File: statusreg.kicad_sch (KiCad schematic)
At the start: 11 parts, among them SW4 SW_DIP_x08, U56 74HC688, U57 74HC573, U58 74HC541, U6 74HC32, U7 74HC14

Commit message: done the pcb layout + added the 1M ram bank project
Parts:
- C17: footprint Capacitor_THT:C_Disc_P2.54mm -> Capacitor_THT:C_Disc_D3.0mm_W1.6mm_P2.54mm
- U56, U57, U58: footprint Package_DIP:DIP-20_W7.62mm_Socket -> Package_DIP:DIP-20_W7.62mm
- U6, U7: footprint Package_DIP:DIP-14_W7.62mm_Socket -> Package_DIP:DIP-14_W7.62mm
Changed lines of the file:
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@@
 			)
 		)
-		(property "Footprint" "Package_DIP:DIP-20_W7.62mm_Socket"
+		(property "Footprint" "Package_DIP:DIP-20_W7.62mm"
 			(at 215.9 76.2 0)
 			(effects
@@
 			)
 		)
-		(property "Footprint" "Package_DIP:DIP-20_W7.62mm_Socket"
+		(property "Footprint" "Package_DIP:DIP-20_W7.62mm"
 			(at 152.4 76.2 0)
 			(effects
@@
 			)
 		)
-		(property "Footprint" "Package_DIP:DIP-20_W7.62mm_Socket"
+		(property "Footprint" "Package_DIP:DIP-20_W7.62mm"
 			(at 88.9 76.2 0)
 			(effects
@@
 			)
 		)
-		(property "Footprint" "Capacitor_THT:C_Disc_P2.54mm"
+		(property "Footprint" "Capacitor_THT:C_Disc_D3.0mm_W1.6mm_P2.54mm"
 			(at 132.08 85.3948 0)
 			(effects
@@
 			)
 		)
-		(property "Footprint" "Package_DIP:DIP-14_W7.62mm_Socket"
+		(property "Footprint" "Package_DIP:DIP-14_W7.62mm"
 			(at 81.28 127 0)
 			(effects
@@
 			)
 		)
-		(property "Footprint" "Package_DIP:DIP-14_W7.62mm_Socket"
+		(property "Footprint" "Package_DIP:DIP-14_W7.62mm"
 			(at 96.52 127 0)
 			(effects

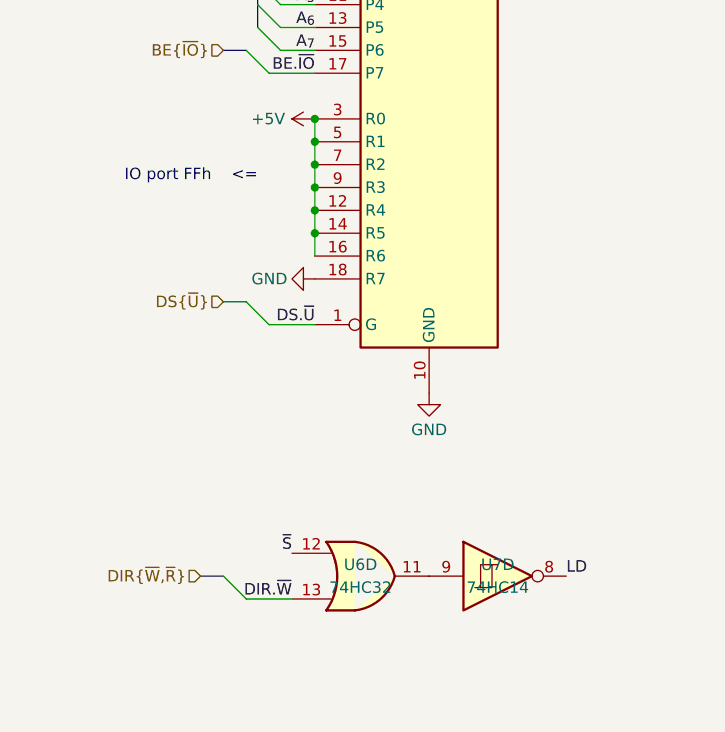
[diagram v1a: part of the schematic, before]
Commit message: updated scheme: 	- fixed E to P & PRT mapping 	- swapped root's 04 couple with the 14's of pidreg & statusreg
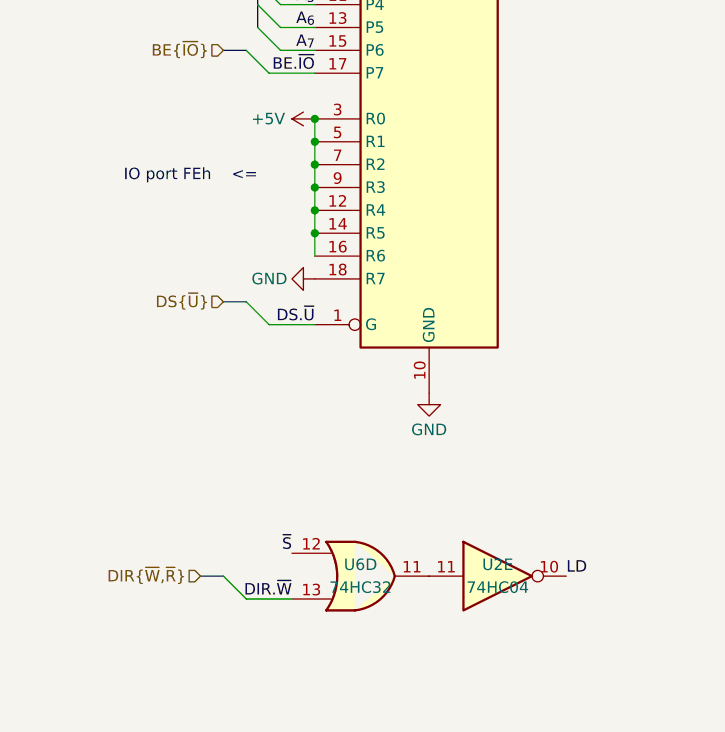
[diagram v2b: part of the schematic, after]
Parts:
- removed U7: 74HC14, Package_DIP:DIP-14_W7.62mm, symbol 74xx:74HC14
- added U2: 74HC04, Package_DIP:DIP-14_W7.62mm, symbol 74xx:74LS04
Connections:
- net LD: now also U2.10
- net at U6.11: now also U2.11
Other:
- note added: "IO port FEh <="
- note removed: "IO port FFh <="
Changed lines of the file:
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@@
 	(generator_version "9.0")
 	(paper "A4")
-	(text "IO port FFh	<="
+	(text "IO port FEh	<="
 		(exclude_from_sim no)
 		(at 69.85 82.55 0)
@@
 	)
 	(symbol
-		(lib_id "74xx:74HC14")
+		(lib_id "74xx:74LS04")
 		(at 96.52 127 0)
-		(unit 4)
+		(unit 5)
 		(exclude_from_sim no)
 		(in_bom yes)
 		(on_board yes)
 		(dnp no)
-		(property "Reference" "U7"
+		(property "Reference" "U2"
 			(at 96.52 125.73 0)
 			(effects
@@
 			)
 		)
-		(property "Value" "74HC14"
+		(property "Value" "74HC04"
 			(at 96.52 128.27 0)
 			(effects
@@
 			)
 		)
-		(property "Datasheet" "http://www.ti.com/lit/gpn/sn74HC14"
+		(property "Datasheet" "http://www.ti.com/lit/gpn/sn74LS04"
 			(at 96.52 127 0)
 			(effects
@@
 			)
 		)
-		(property "Description" "Hex inverter schmitt trigger"
+		(property "Description" "Hex Inverter"
 			(at 96.52 127 0)
 			(effects
@@
 			)
 		)
-		(pin "1"
+		(pin "11"
 		)
-		(pin "5"
+		(pin "7"
 		)
-		(pin "6"
+		(pin "5"
 		)
 		(pin "4"
 		)
-		(pin "2"
+		(pin "3"
 		)
-		(pin "8"
+		(pin "2"
 		)
 		(pin "9"
 		)
-		(pin "3"
+		(pin "14"
 		)
-		(pin "12"
+		(pin "6"
 		)
-		(pin "10"
+		(pin "1"
 		)
-		(pin "7"
+		(pin "8"
 		)
-		(pin "13"
+		(pin "10"
 		)
-		(pin "14"
+		(pin "12"
 		)
-		(pin "11"
+		(pin "13"
 		)
 		(instances
 			(project "SCRM6816"
 				(path "/56448118-82b3-4e1c-bda3-84d63e01a14a/6b7efd4b-9562-42f4-9e10-c9325680e8f3"
-					(reference "U7")
-					(unit 4)
+					(reference "U2")
+					(unit 5)
 				)
 			)

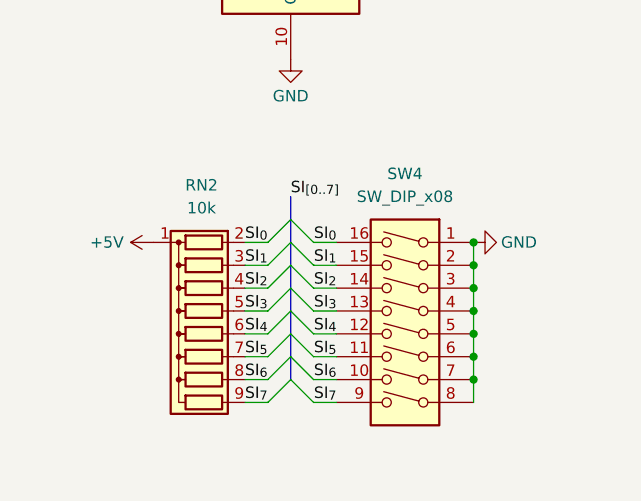
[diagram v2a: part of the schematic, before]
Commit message: apparently the ram was enabled all the time, ram.kicad_sch didn't even require BE.M... 	like whaaaaaaaa how did i let this happen oh my god sometimes im just braindead.
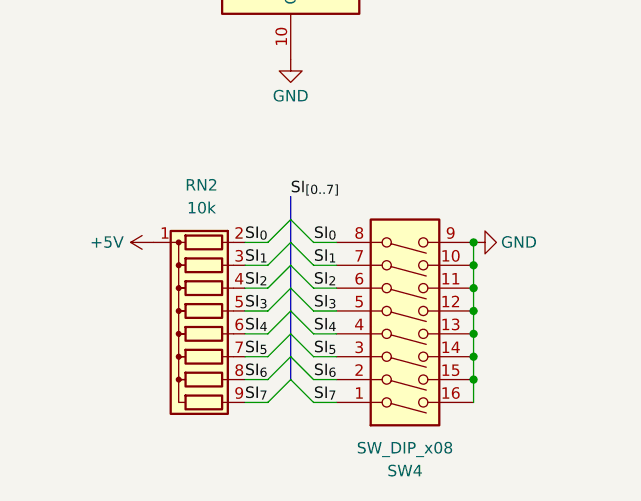
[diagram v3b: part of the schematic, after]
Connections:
- net GND: now also SW4.10, SW4.11, SW4.12, SW4.13, SW4.14, SW4.15, SW4.16, SW4.9; no longer SW4.1, SW4.2, SW4.3, SW4.4, SW4.5, SW4.6, SW4.7, SW4.8
- net SI_{0}: now also SW4.8; no longer SW4.16
- net SI_{1}: now also SW4.7; no longer SW4.15
- net SI_{2}: now also SW4.6; no longer SW4.14
- net SI_{3}: now also SW4.5; no longer SW4.13
- net SI_{4}: now also SW4.4; no longer SW4.12
- net SI_{5}: now also SW4.3; no longer SW4.11
- net SI_{6}: now also SW4.2; no longer SW4.10
- net SI_{7}: now also SW4.1; no longer SW4.9
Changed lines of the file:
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@@
 	(symbol
 		(lib_id "Switch:SW_DIP_x08")
-		(at 228.6 127 0)
-		(mirror y)
+		(at 228.6 124.46 0)
+		(mirror x)
 		(unit 1)
 		(exclude_from_sim no)
@@
 		(dnp no)
 		(property "Reference" "SW4"
-			(at 228.6 109.22 0)
+			(at 228.6 142.24 0)
 			(effects
 				(font
@@
 		)
 		(property "Value" "SW_DIP_x08"
-			(at 228.6 111.76 0)
+			(at 228.6 139.7 0)
 			(effects
 				(font
@@
 		)
 		(property "Footprint" "Button_Switch_THT:SW_DIP_SPSTx08_Slide_9.78x22.5mm_W7.62mm_P2.54mm"
-			(at 228.6 127 0)
+			(at 228.6 124.46 0)
 			(effects
 				(font
@@
 		)
 		(property "Datasheet" "~"
-			(at 228.6 127 0)
+			(at 228.6 124.46 0)
 			(effects
 				(font
@@
 		)
 		(property "Description" "8x DIP Switch, Single Pole Single Throw (SPST) switch, small symbol"
-			(at 228.6 127 0)
+			(at 228.6 124.46 0)
 			(effects
 				(font

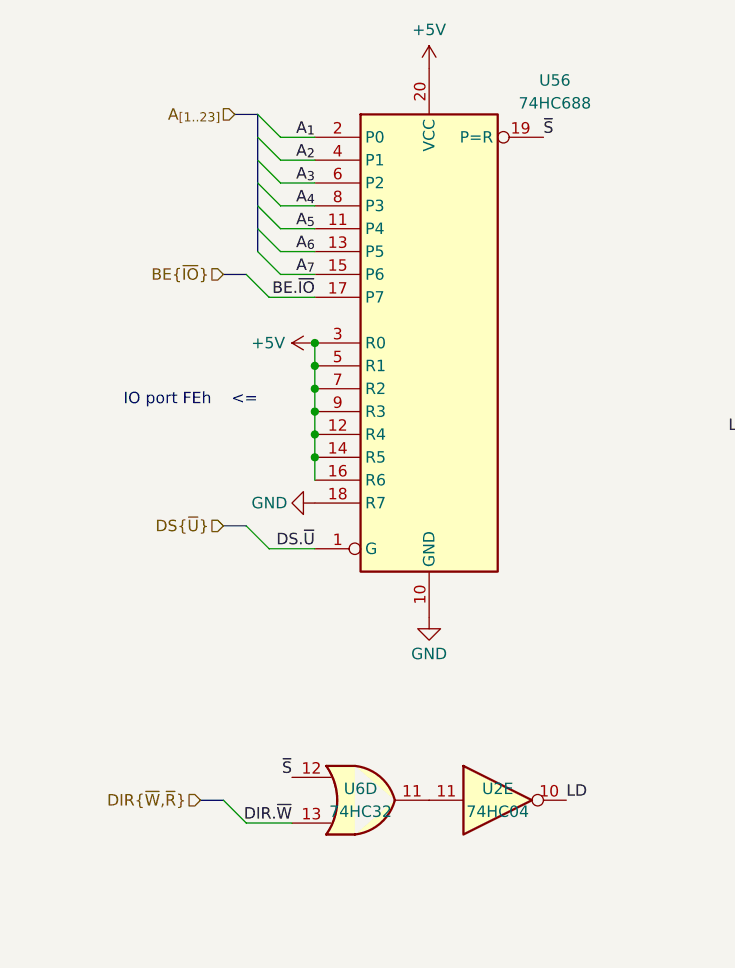
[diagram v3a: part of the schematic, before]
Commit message: first commit: scheme ok [decoder]: 	- new spv. address space [mmu]: 	- removed pidreg 	- switched back to 8Kb mmu rams [ram/peripherals]: 	- added ground pins to connectors [misc]: 	- added DMA support 	- added clock halfer
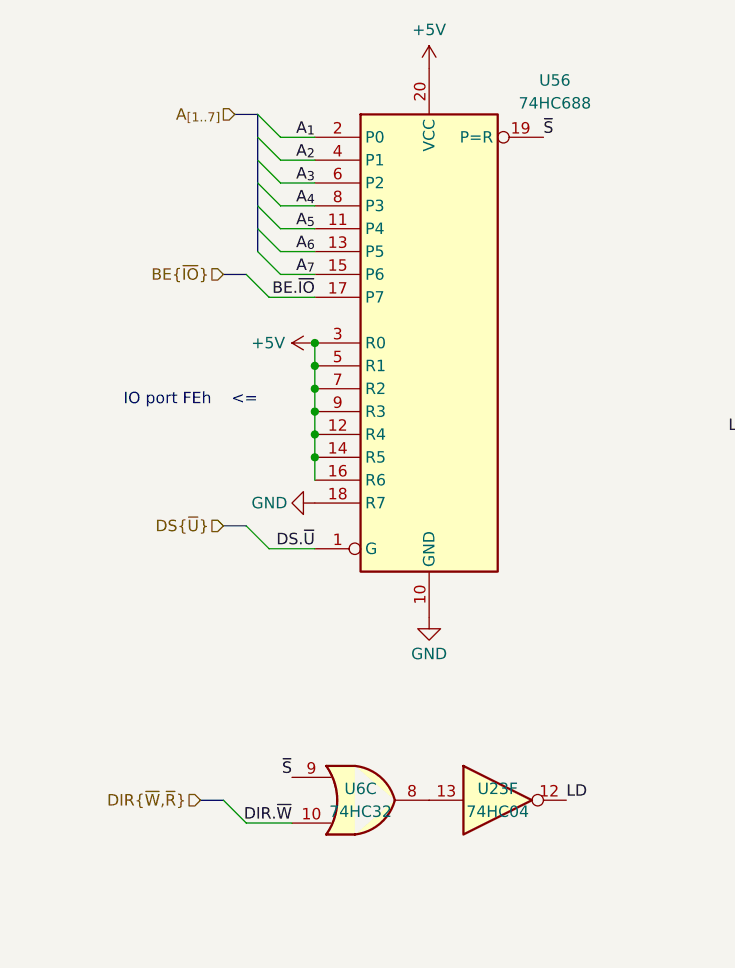
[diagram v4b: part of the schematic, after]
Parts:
- removed U2: 74HC04, Package_DIP:DIP-14_W7.62mm, symbol 74xx:74LS04
- removed U6: 74HC32, Package_DIP:DIP-14_W7.62mm, symbol 74xx:74LS32
- added U23: 74HC04, symbol 74xx:74LS04
- added U6: 74HC32, Package_DIP:DIP-14_W7.62mm, symbol 74xx:74LS32
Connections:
- net DIR.~{W}: now also U6.10
- net LD: now also U23.12
- net ~{S}: now also U6.9
- new net: U23.13, U6.8
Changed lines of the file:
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@@
 		)
 	)
-	(hierarchical_label "A_{[1..23]}"
+	(hierarchical_label "A_{[1..7]}"
 		(shape input)
 		(at 67.31 50.8 180)
@@
 	)
 	(symbol
+		(lib_id "74xx:74LS04")
+		(at 96.52 127 0)
+		(unit 6)
+		(exclude_from_sim no)
+		(in_bom yes)
+		(on_board yes)
+		(dnp no)
+		(property "Reference" "U23"
+			(at 96.52 125.73 0)
+			(effects
+				(font
+					(size 1.27 1.27)
+				)
+			)
+		)
+		(property "Value" "74HC04"
+			(at 96.52 128.27 0)
+			(effects
+				(font
+					(size 1.27 1.27)
+				)
+			)
+		)
+		(property "Footprint" ""
+			(at 96.52 127 0)
+			(effects
+				(font
+					(size 1.27 1.27)
+				)
+				(hide yes)
+			)
+		)
+		(property "Datasheet" "http://www.ti.com/lit/gpn/sn74LS04"
+			(at 96.52 127 0)
+			(effects
+				(font
+					(size 1.27 1.27)
+				)
+				(hide yes)
+			)
+		)
+		(property "Description" "Hex Inverter"
+			(at 96.52 127 0)
+			(effects
+				(font
+					(size 1.27 1.27)
+				)
+				(hide yes)
+			)
+		)
+		(pin "5"
+		)
+		(pin "4"
+		)
+		(pin "13"
+		)
+		(pin "1"
+		)
+		(pin "14"
+		)
+		(pin "3"
+		)
+		(pin "6"
+		)
+		(pin "8"
+		)
+		(pin "11"
+		)
+		(pin "12"
+		)
+		(pin "7"
+		)
+		(pin "2"
+		)
+		(pin "9"
+		)
+		(pin "10"
+		)
+		(instances
+			(project "SCRM6816"
+				(path "/56448118-82b3-4e1c-bda3-84d63e01a14a/6b7efd4b-9562-42f4-9e10-c9325680e8f3"
+					(reference "U23")
+					(unit 6)
+				)
+			)
+		)
+	)
+	(symbol
 		(lib_id "power:GND")
 		(at 76.2 93.98 270)
@@
 	)
 	(symbol
+		(lib_id "74xx:74LS32")
+		(at 81.28 127 0)
+		(unit 3)
+		(exclude_from_sim no)
+		(in_bom yes)
+		(on_board yes)
+		(dnp no)
+		(property "Reference" "U6"
+			(at 81.28 125.73 0)
+			(effects
+				(font
+					(size 1.27 1.27)
+				)
+			)
+		)
+		(property "Value" "74HC32"
+			(at 81.28 128.27 0)
+			(effects
+				(font
+					(size 1.27 1.27)
+				)
+			)
+		)
+		(property "Footprint" "Package_DIP:DIP-14_W7.62mm"
+			(at 81.28 127 0)
+			(effects
+				(font
+					(size 1.27 1.27)
+				)
+				(hide yes)
+			)
+		)
+		(property "Datasheet" "http://www.ti.com/lit/gpn/sn74LS32"
+			(at 81.28 127 0)
+			(effects
+				(font
+					(size 1.27 1.27)
+				)
+				(hide yes)
+			)
+		)
+		(property "Description" "Quad 2-input OR"
+			(at 81.28 127 0)
+			(effects
+				(font
+					(size 1.27 1.27)
+				)
+				(hide yes)
+			)
+		)
+		(pin "7"
+		)
+		(pin "2"
+		)
+		(pin "3"
+		)
+		(pin "5"
+		)
+		(pin "9"
+		)
+		(pin "11"
+		)
+		(pin "8"
+		)
+		(pin "12"
+		)
+		(pin "14"
+		)
+		(pin "13"
+		)
+		(pin "10"
+		)
+		(pin "1"
+		)
+		(pin "4"
+		)
+		(pin "6"
+		)
+		(instances
+			(project "SCRM6816"
+				(path "/56448118-82b3-4e1c-bda3-84d63e01a14a/6b7efd4b-9562-42f4-9e10-c9325680e8f3"
+					(reference "U6")
+					(unit 3)
+				)
+			)
+		)
+	)
+	(symbol
 		(lib_id "power:GND")
 		(at 132.08 93.98 0)
@@
 	)
 	(symbol
-		(lib_id "74xx:74LS32")
-		(at 81.28 127 0)
-		(unit 4)
-		(exclude_from_sim no)
-		(in_bom yes)
-		(on_board yes)
-		(dnp no)
-		(property "Reference" "U6"
-			(at 81.28 125.73 0)
-			(effects
-				(font
-					(size 1.27 1.27)
-				)
-			)
-		)
-		(property "Value" "74HC32"
-			(at 81.28 128.27 0)
-			(effects
-				(font
-					(size 1.27 1.27)
-				)
-			)
-		)
-		(property "Footprint" "Package_DIP:DIP-14_W7.62mm"
-			(at 81.28 127 0)
-			(effects
-				(font
-					(size 1.27 1.27)
-				)
-				(hide yes)
-			)
-		)
-		(property "Datasheet" "http://www.ti.com/lit/gpn/sn74LS32"
-			(at 81.28 127 0)
-			(effects
-				(font
-					(size 1.27 1.27)
-				)
-				(hide yes)
-			)
-		)
-		(property "Description" "Quad 2-input OR"
-			(at 81.28 127 0)
-			(effects
-				(font
-					(size 1.27 1.27)
-				)
-				(hide yes)
-			)
-		)
-		(pin "7"
-		)
-		(pin "2"
-		)
-		(pin "3"
-		)
-		(pin "5"
-		)
-		(pin "9"
-		)
-		(pin "11"
-		)
-		(pin "8"
-		)
-		(pin "12"
-		)
-		(pin "14"
-		)
-		(pin "13"
-		)
-		(pin "10"
-		)
-		(pin "1"
-		)
-		(pin "4"
-		)
-		(pin "6"
-		)
-		(instances
-			(project "SCRM6816"
-				(path "/56448118-82b3-4e1c-bda3-84d63e01a14a/6b7efd4b-9562-42f4-9e10-c9325680e8f3"
-					(reference "U6")
-					(unit 4)
-				)
-			)
-		)
-	)
-	(symbol
 		(lib_id "power:+9V")
 		(at 152.4 55.88 0)
@@
 				)
 			)
-		)
-	)
-	(symbol
-		(lib_id "74xx:74LS04")
-		(at 96.52 127 0)
-		(unit 5)
-		(exclude_from_sim no)
-		(in_bom yes)
-		(on_board yes)
-		(dnp no)
-		(property "Reference" "U2"
-			(at 96.52 125.73 0)
-			(effects
-				(font
-					(size 1.27 1.27)
-				)
-			)
-		)
-		(property "Value" "74HC04"
-			(at 96.52 128.27 0)
-			(effects
-				(font
-					(size 1.27 1.27)
-				)
-			)
-		)
-		(property "Footprint" "Package_DIP:DIP-14_W7.62mm"
-			(at 96.52 127 0)
-			(effects
-				(font
-					(size 1.27 1.27)
-				)
-				(hide yes)
-			)
-		)
-		(property "Datasheet" "http://www.ti.com/lit/gpn/sn74LS04"
-			(at 96.52 127 0)
-			(effects
-				(font
-					(size 1.27 1.27)
-				)
-				(hide yes)
-			)
-		)
-		(property "Description" "Hex Inverter"
-			(at 96.52 127 0)
-			(effects
-				(font
-					(size 1.27 1.27)
-				)
-				(hide yes)
-			)
-		)
-		(pin "11"
-		)
-		(pin "7"
-		)
-		(pin "5"
-		)
-		(pin "4"
-		)
-		(pin "3"
-		)
-		(pin "2"
-		)
-		(pin "9"
-		)
-		(pin "14"
-		)
-		(pin "6"
-		)
-		(pin "1"
-		)
-		(pin "8"
-		)
-		(pin "10"
-		)
-		(pin "12"
-		)
-		(pin "13"
-		)
-		(instances
-			(project "SCRM6816"
-				(path "/56448118-82b3-4e1c-bda3-84d63e01a14a/6b7efd4b-9562-42f4-9e10-c9325680e8f3"
-					(reference "U2")
-					(unit 5)
-				)
-			)

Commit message: assigned footprints
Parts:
- U23: footprint (none) -> Package_DIP:DIP-14_W7.62mm
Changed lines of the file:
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@@
 			)
 		)
-		(property "Footprint" ""
+		(property "Footprint" "Package_DIP:DIP-14_W7.62mm"
 			(at 96.52 127 0)
 			(effects
